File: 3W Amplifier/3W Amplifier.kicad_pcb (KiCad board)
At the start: 2 copper layers, 26 parts, among them U1 PAM8008

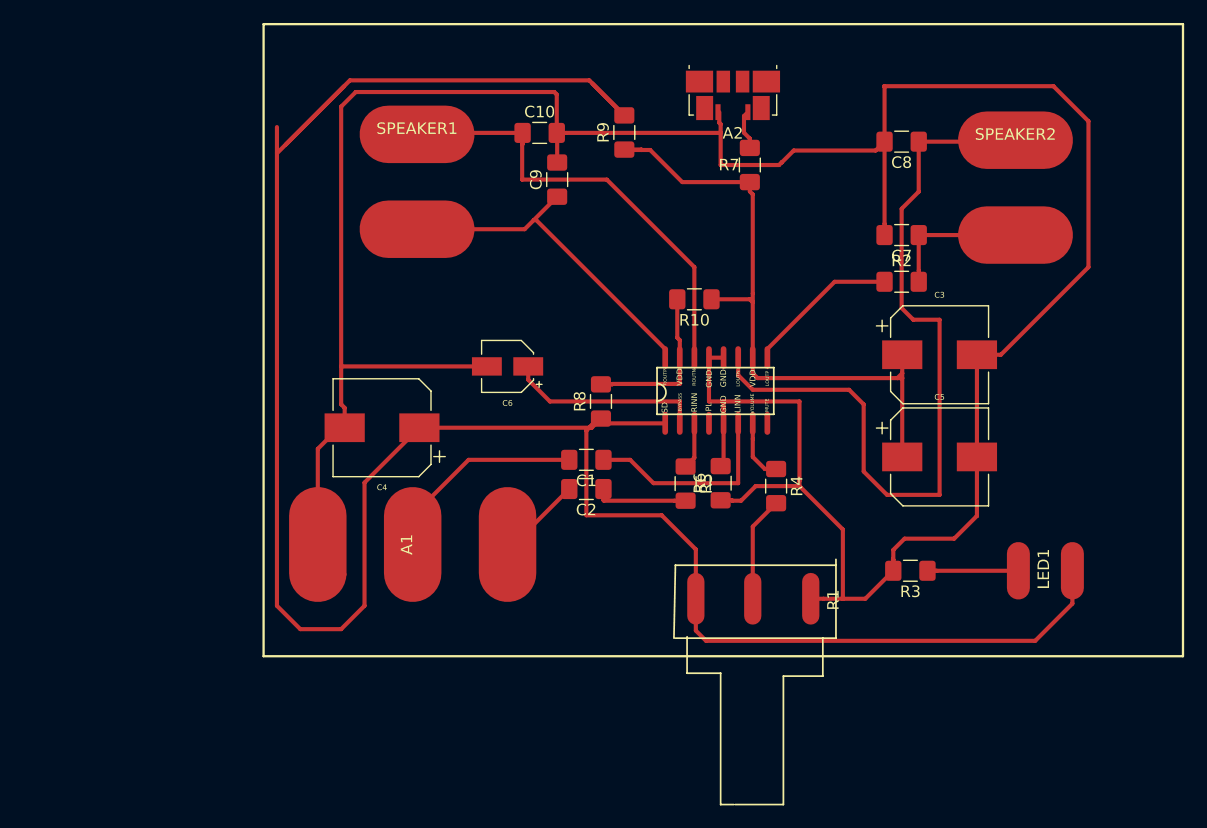
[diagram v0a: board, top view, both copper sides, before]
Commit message: bring in new parts and delete all tracks
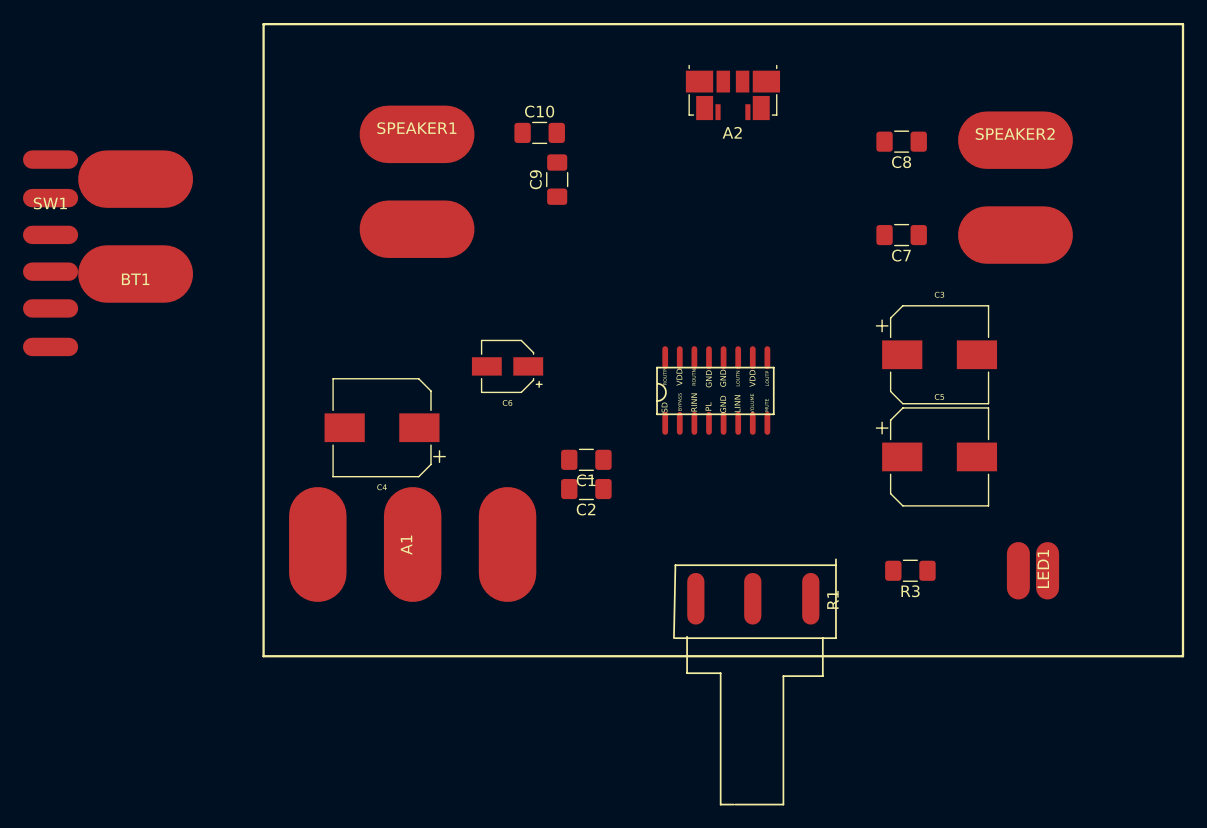
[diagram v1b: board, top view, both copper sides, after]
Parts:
- removed R10, R2, R4, R5, R6, R7, R8, R9: 0Ω, NewFootPrint:Resistor
- added BT1: Battery, NewFootPrint:Speaker, F.Cu at (13.9, 41.7)
- added SW1: SW_DIP_x02, NewFootPrint:Switch-ES02MSABE, F.Cu at (6.46, 35.1)
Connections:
- A1 pad S: Net-(A1-PadS) -> /GND
- A1 pad T: /GND -> Net-(A1-PadT)
- A2 pad 1: Net-(A2-Pad1) -> (no net)
- C1 pad 2: Net-(A1-PadR) -> Net-(A1-PadT)
- C2 pad 2: Net-(A1-PadS) -> Net-(A1-PadR)
- LED1 pad 1: Net-(LED1-Pad1) -> (no net)
- U1 pad 2: /BYPASS -> (no net)
- U1 pad 3: Net-(R5-Pad1) -> /RINN
- U1 pad 4: Net-(U1-Pad4) -> (no net)
- U1 pad 7: /VOLUME -> (no net)
- U1 pad 8: Net-(U1-Pad8) -> (no net)
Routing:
- net /GND: track 247.7 -> 0.00 mm
- net /VDD: track 235.0 -> 0.00 mm
- net /LOUTN: track 69.3 -> 0.00 mm
- net /ROUTN: track 39.3 -> 0.00 mm
- net Net-(C4-Pad1): track 37.0 -> 0.00 mm
- net /ROUTP: track 30.2 -> 0.00 mm
- net /LOUTP: track 25.9 -> 0.00 mm
- net Net-(A1-PadR): track 20.6 -> 0.00 mm
- net /LINN: track 17.8 -> 0.00 mm
- net /BYPASS: track 17.0 -> 0.00 mm
- net Net-(R1-Pad2): track 9.16 -> 0.00 mm
- net Net-(LED1-Pad1): track 8.72 -> 0.00 mm
- net /RINN: track 8.14 -> 0.00 mm
- net Net-(A1-PadS): track 7.37 -> 0.00 mm
- net /VOLUME: track 5.39 -> 0.00 mm
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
